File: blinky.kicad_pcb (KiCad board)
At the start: 2 copper layers, 69.9 x 70 mm, 68 parts, among them J1 MIC_CLK, J10 DEBUG, J11 SWD, J12 BATTERY, J13 UART, J14 5V, J15 3V3, J16 GS2, J17 GS2, J2 MIC_DOUT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

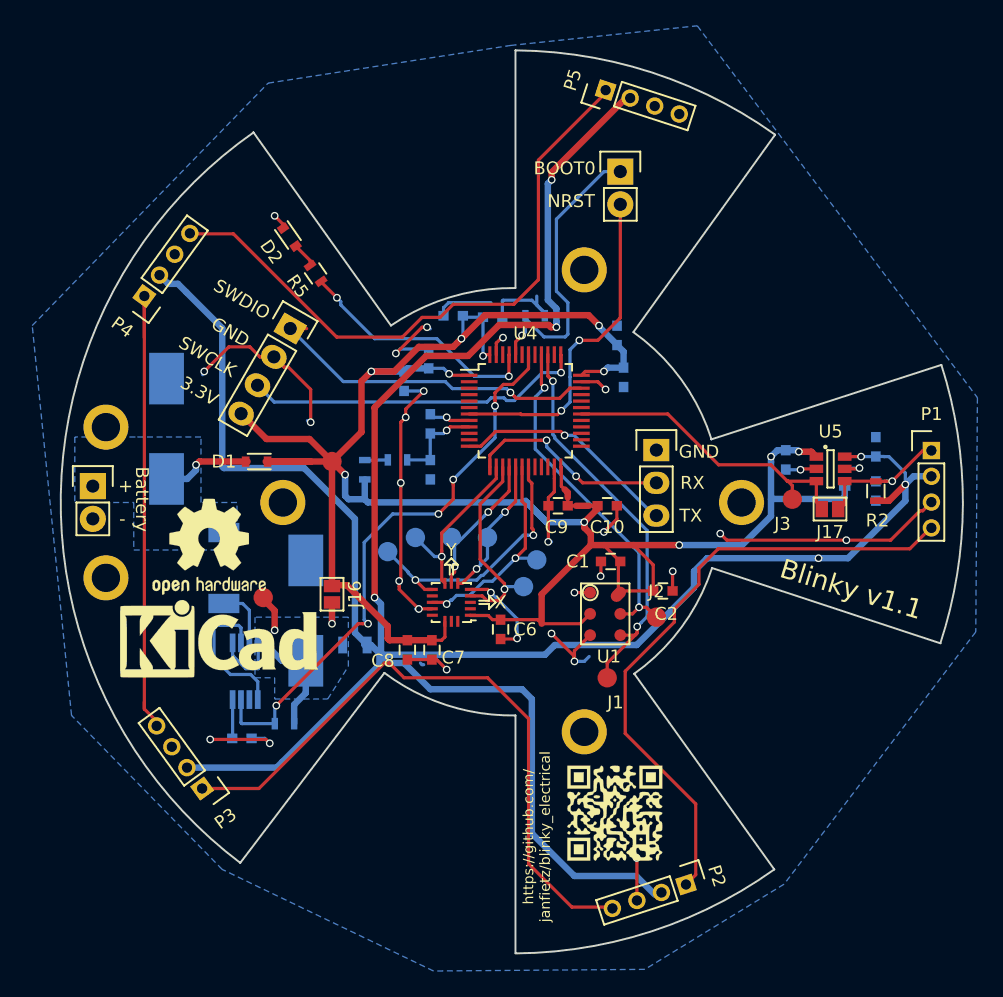
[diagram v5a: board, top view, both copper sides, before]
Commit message: new led pin footprints
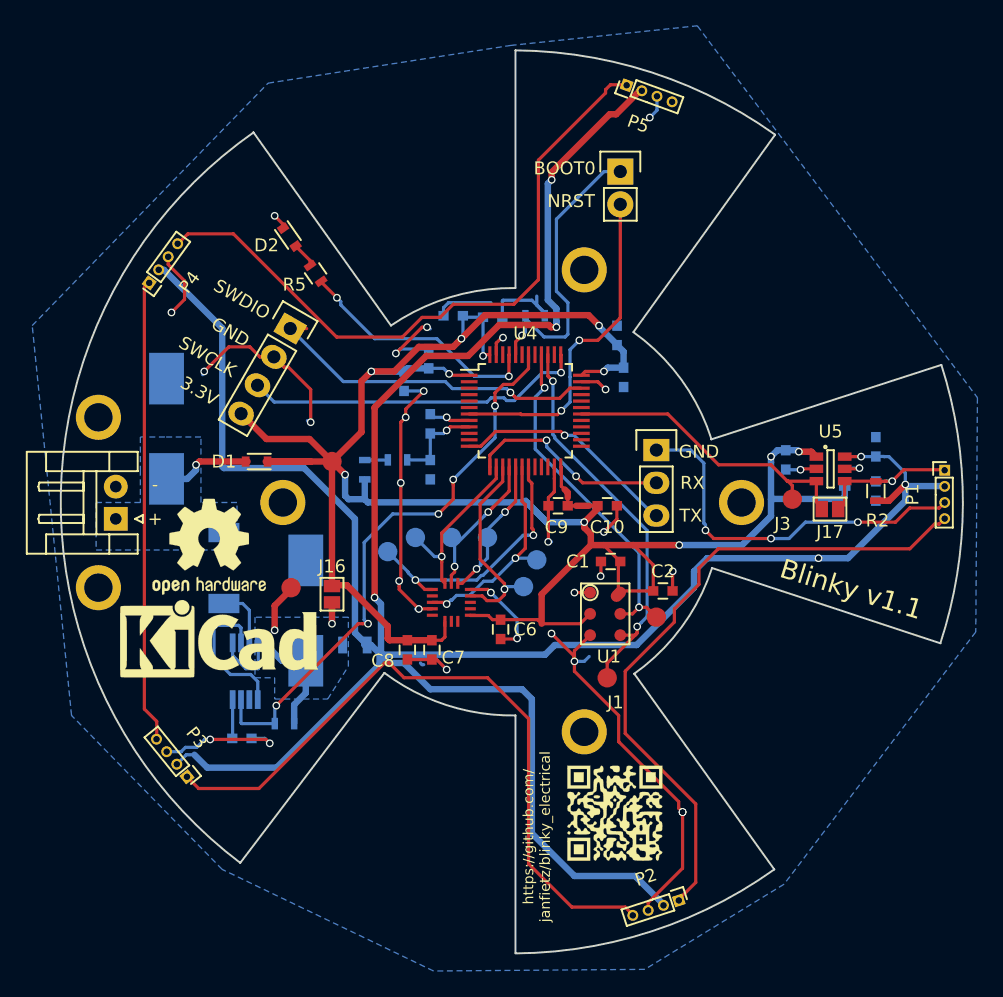
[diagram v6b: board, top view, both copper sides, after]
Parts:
- J12: footprint Pin_Headers:Pin_Header_Straight_1x02 -> Connectors_JST:JST_EH_S02B-EH_02x2.50mm_Angled
- P1, P2, P3, P4, P5: footprint Pin_Headers:Pin_Header_Straight_1x04_Pitch2.00mm -> jfi:Pin_Header_Straight_1_04_Pitch1.25mm
- U3: footprint LGA-16-3x3_Axis -> tinkerforge:LGA-16-3x3
- moved J12 3.10 mm to (101.3, 74.9), turned to 90 degrees
- moved J14 2.29 mm to (114.9, 80.3)
- moved P1 1.84 mm to (165.6, 71.2), turned to 270 degrees
- moved P5 1.67 mm to (141.0, 41.3), turned to 340 degrees
- moved P3 1.49 mm to (106.9, 94.9), turned to 129 degrees
- moved P2 1.35 mm to (145.0, 104.5), turned to 198 degrees
- moved P4 1.09 mm to (103.9, 56.6), turned to 54 degrees
- moved REF** 0.96 mm to (100.0, 67.1)
- moved REF** 0.96 mm to (100.0, 80.3)
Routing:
- net GND: track 132.1 -> 175.1 mm, vias 30 -> 34
- net /LED_5V: track 211.8 -> 216.0 mm
- net Net-(P2-Pad4): track 50.2 -> 53.8 mm
- net Net-(P4-Pad4): track 49.1 -> 52.1 mm
- net Net-(P1-Pad4): track 48.8 -> 51.5 mm
- net Net-(P3-Pad4): track 38.4 -> 36.5 mm
- net +5V: track 21.0 -> 21.9 mm
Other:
- board text removed: "Battery"
